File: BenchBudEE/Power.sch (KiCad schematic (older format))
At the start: 0 parts

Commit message: swapping Power and PowerAdjustmentMonitor schematics
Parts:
- added C?: 5566-20A, ~, symbol 5566-20A
- added F? (x6): FUSE, ~, symbol FUSE
- added SW?: SWITCH_INV, ~, symbol SWITCH_INV
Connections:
- new net: C?.1 (+3.3V), C?.11 (+3.3V_SENSE), C?.2 (+3.3V), F?.1
- new net: C?.10 (+12V), F?.2
- new net: C?.12 (-12V), F?.1
- new net: C?.18 (-5V_OPT), F?.1
- new net: C?.19 (+5V), C?.20 (+5V), C?.4 (+5V), C?.6 (+5V), F?.2
- new net +12V: F?.1
- new net +3.3V: F?.2
- new net +5V: F?.1
- new net -12V: F?.2
- new net -5V: F?.2
- new net GND: C?.13 (GND), C?.15 (GND), C?.16 (GND), C?.17 (GND), C?.3 (GND), C?.5 (GND), C?.7 (GND)

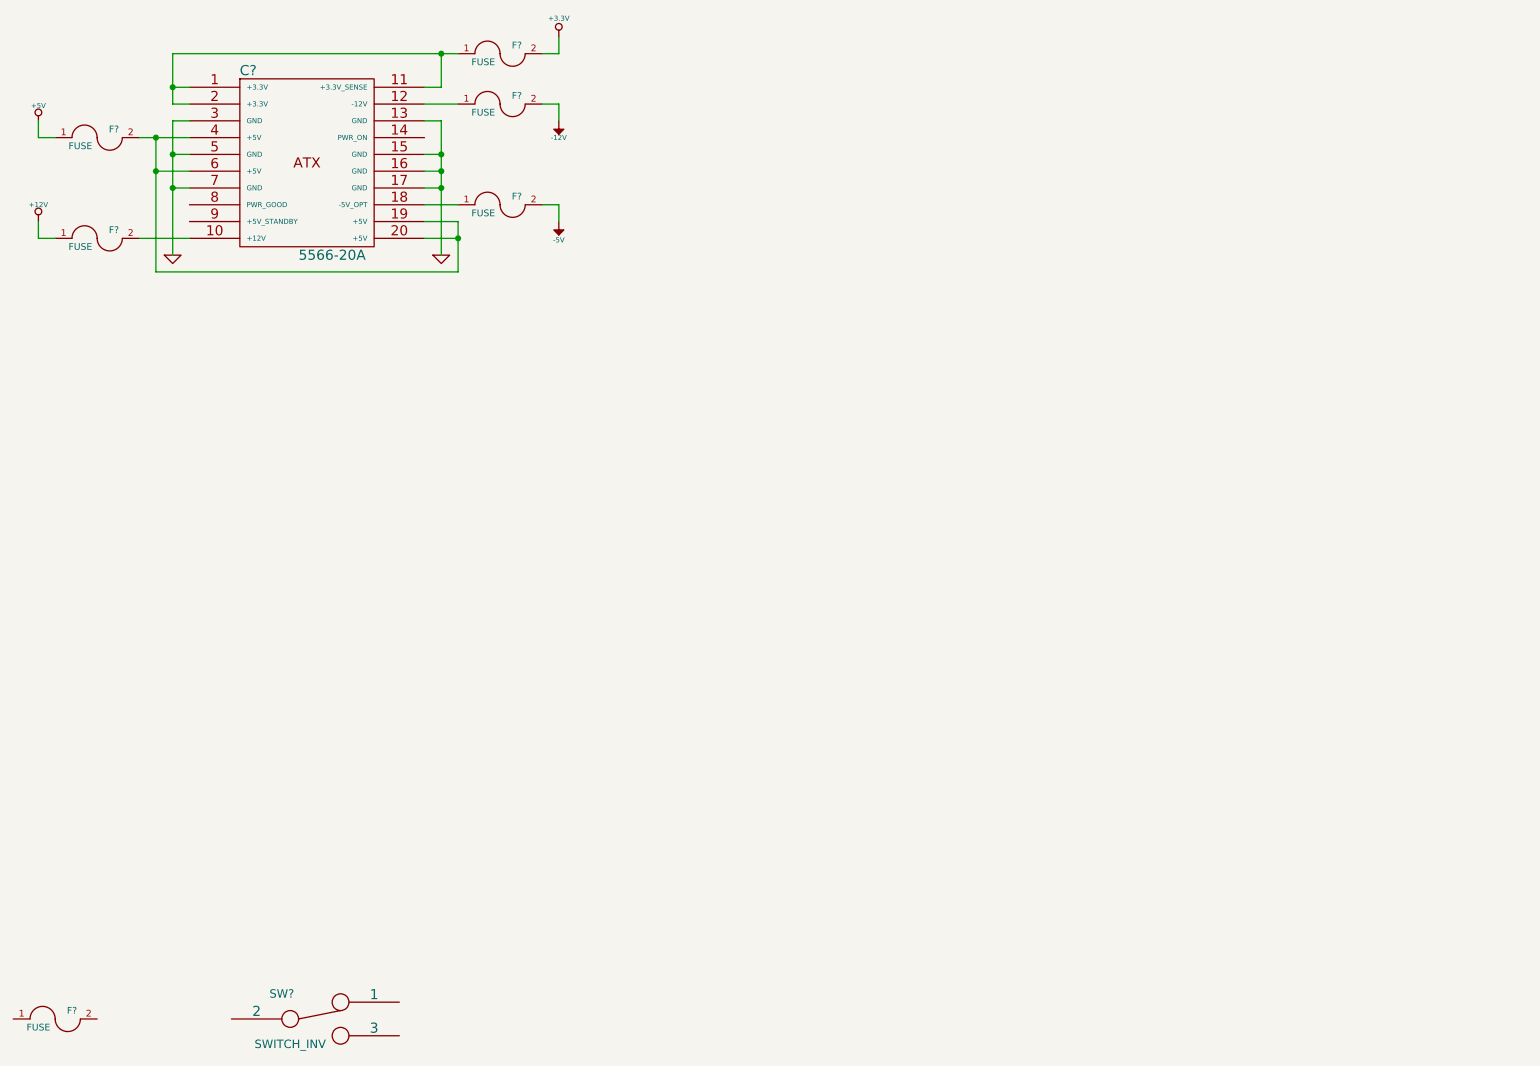
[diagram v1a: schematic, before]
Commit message: Implementing the Power schematic.
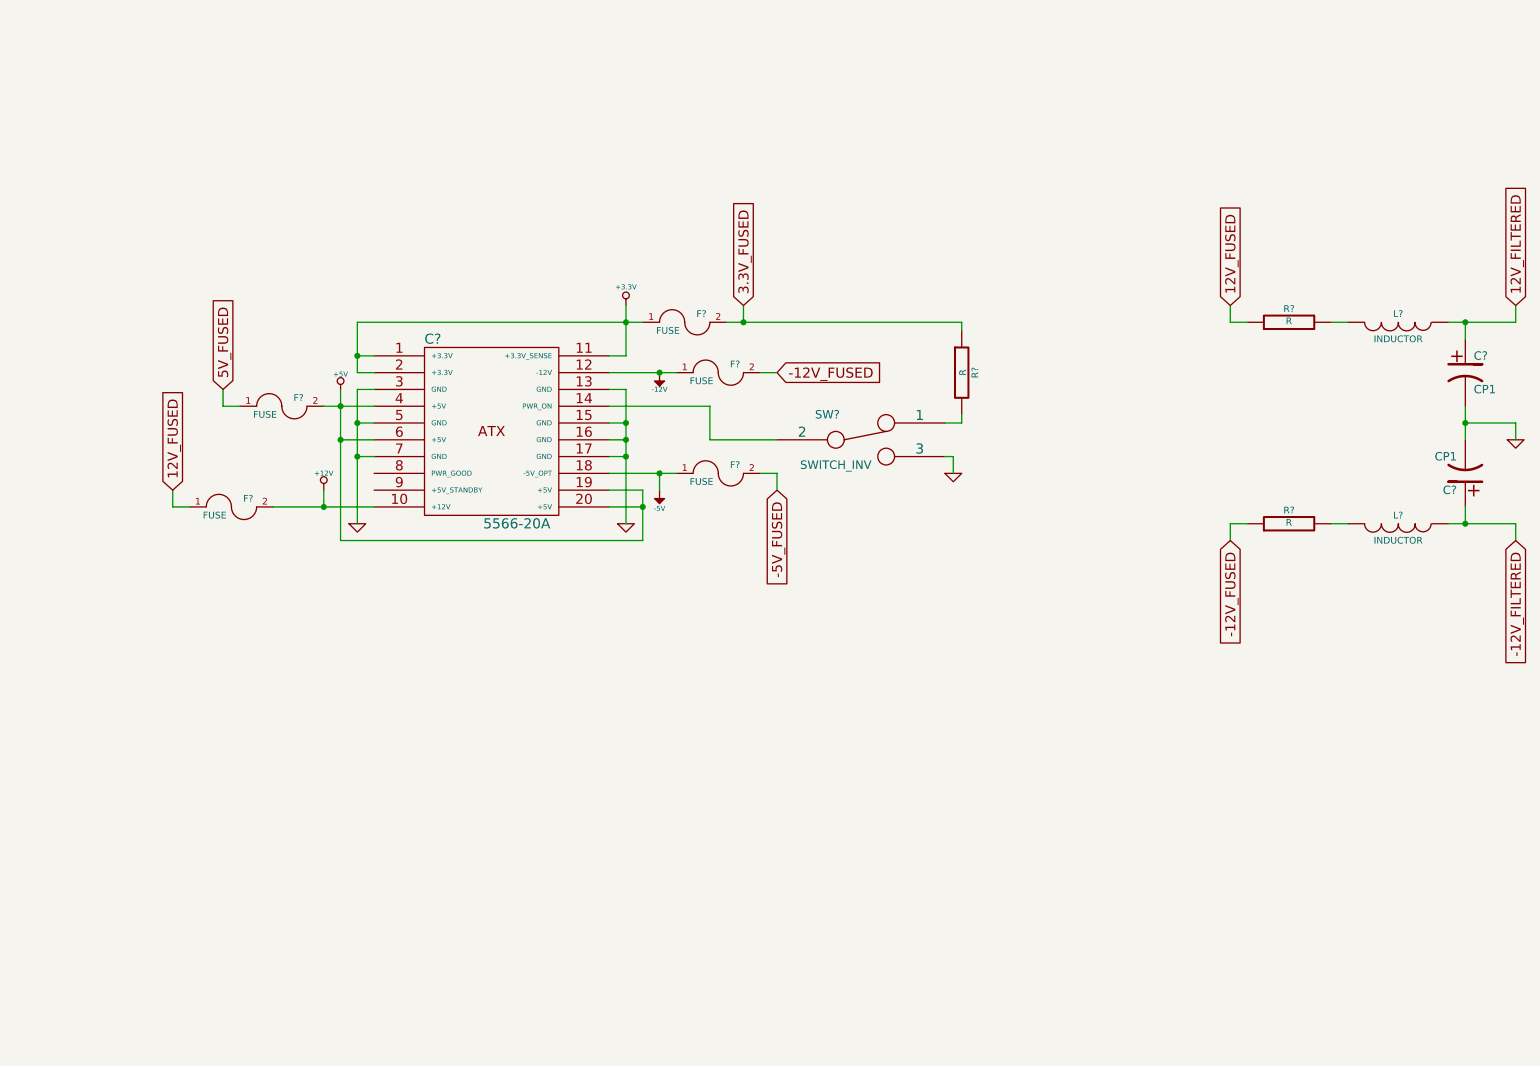
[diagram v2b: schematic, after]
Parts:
- removed F?: FUSE, ~, symbol FUSE
- added C? (x2): CP1, ~, symbol CP1
- added L? (x2): INDUCTOR, ~, symbol INDUCTOR
- added R? (x3): R, ~, symbol R
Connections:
- net +12V: now also C?.10 (+12V), F?.2; no longer F?.1
- net +3.3V: now also C?.1 (+3.3V), C?.11 (+3.3V_SENSE), C?.2 (+3.3V), F?.1; no longer F?.2
- net +5V: now also C?.19 (+5V), C?.20 (+5V), C?.4 (+5V), C?.6 (+5V), F?.2; no longer F?.1
- net -12V: now also C?.12 (-12V), F?.1; no longer F?.2
- net -5V: now also C?.18 (-5V_OPT), F?.1; no longer F?.2
- net GND: now also SW?.3, C?.2, C?.2
- net at C?.14 (PWR_ON): now also SW?.2
- net at SW?.1: now also R?.2
- new net: L?.2, R?.2 (x2)
- new net -12V_FILTERED: C?.1, L?.1
- new net -12V_FUSED: F?.2, R?.1
- new net -5V_FUSED: F?.2
- new net 12V_FILTERED: C?.1, L?.1
- new net 12V_FUSED: F?.1, R?.1
- new net 3.3V_FUSED: F?.2, R?.1
- new net 5V_FUSED: F?.1
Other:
- moved on the sheet: C?, F?, SW?

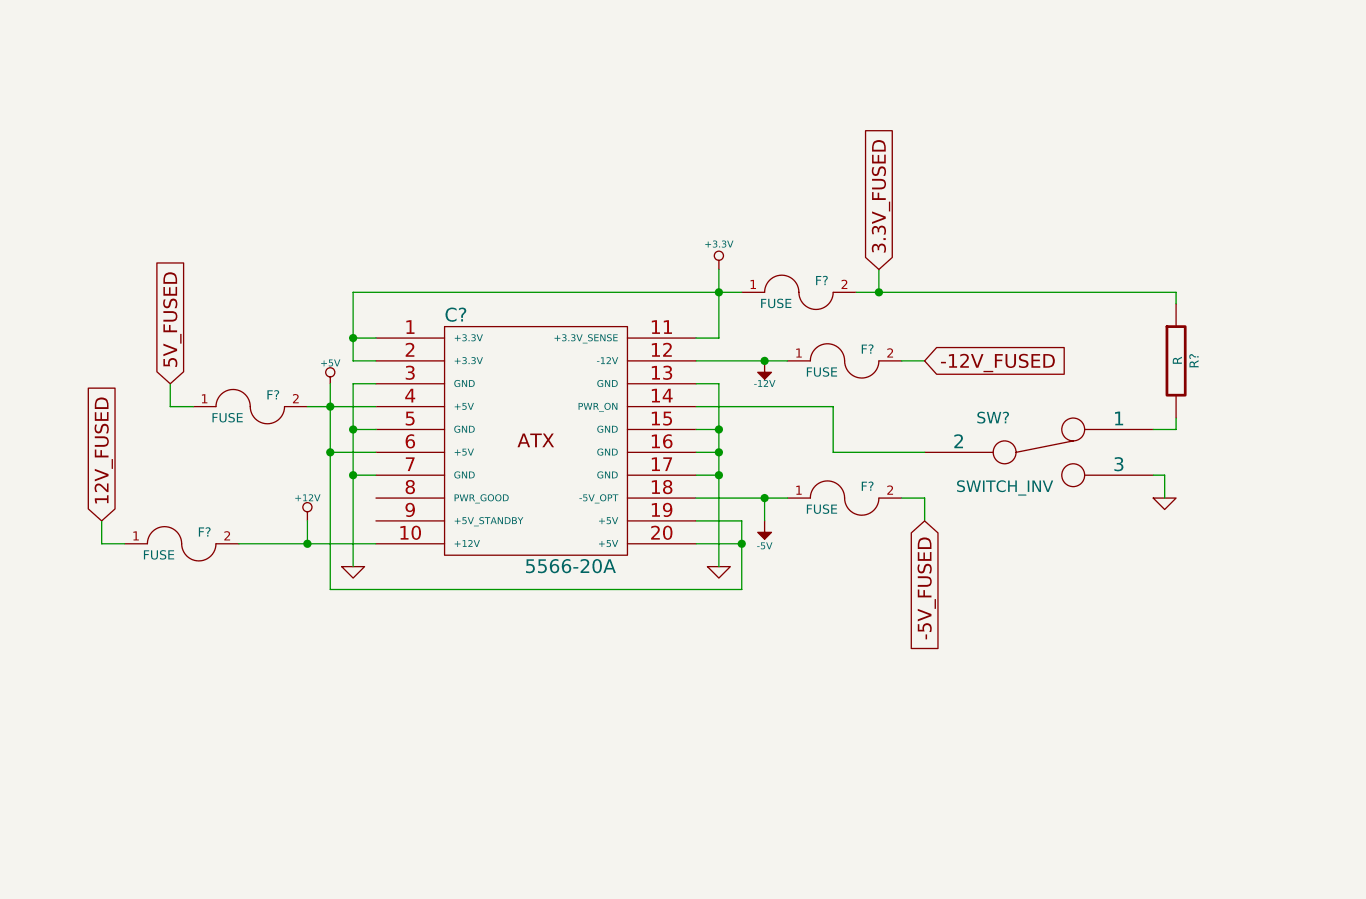
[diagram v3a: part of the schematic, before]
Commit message: Completing schematics from week 3 videos.
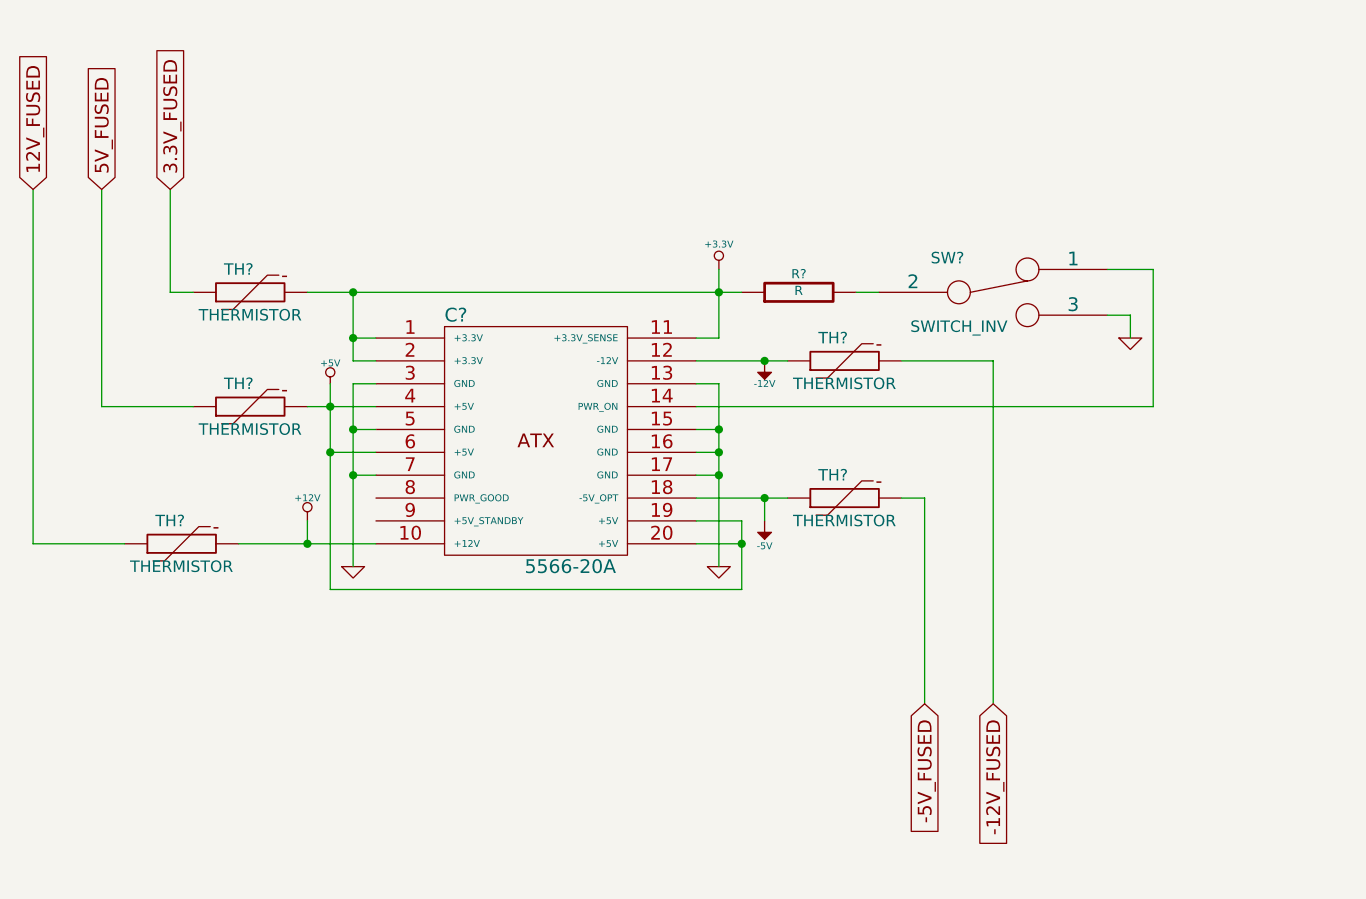
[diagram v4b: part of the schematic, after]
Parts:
- removed F? (x5): FUSE, ~, symbol FUSE
- added TH? (x5): THERMISTOR, ~, symbol THERMISTOR
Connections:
- net +12V: now also TH?.2
- net +3.3V: now also R?.1, TH?.2
- net +5V: now also TH?.2
- net -12V: now also TH?.1
- net -12V_FUSED: now also TH?.2
- net -5V: now also TH?.1
- net -5V_FUSED: now also TH?.2
- net 12V_FUSED: now also TH?.1
- net 3.3V_FUSED: now also TH?.1; no longer R?.1
- net 5V_FUSED: now also TH?.1
- net at C?.14 (PWR_ON): now also SW?.1; no longer SW?.2
- net at R?.2: now also SW?.2; no longer SW?.1
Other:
- moved on the sheet: R?, SW?
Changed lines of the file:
@@
 LIBS:relay_spdt
 LIBS:5566-20A
+LIBS:AP5726
+LIBS:arduino
 LIBS:BenchBudEE-cache
 EELAYER 27 0
@@
 $Descr A4 11693 8268
 encoding utf-8
-Sheet 5 9
+Sheet 4 9
 Title ""
-Date "13 feb 2014"
+Date "24 feb 2014"
 Rev ""
 Comp ""
@@
 L SWITCH_INV SW?
 U 1 1 52FAF3C7
-P 6050 3800
-F 0 "SW?" H 5850 3950 50  0000 C CNN
-F 1 "SWITCH_INV" H 5900 3650 50  0000 C CNN
-F 2 "~" H 6050 3800 60  0000 C CNN
-F 3 "~" H 6050 3800 60  0000 C CNN
-	1    6050 3800
-	1    0    0    -1
-$EndComp
-$Comp
-L FUSE F?
-U 1 1 52FAF3D4
-P 5000 3100
-F 0 "F?" H 5100 3150 40  0000 C CNN
-F 1 "FUSE" H 4900 3050 40  0000 C CNN
-F 2 "~" H 5000 3100 60  0000 C CNN
-F 3 "~" H 5000 3100 60  0000 C CNN
-	1    5000 3100
-	1    0    0    -1
-$EndComp
-$Comp
-L FUSE F?
-U 1 1 52FAF44C
-P 2600 3600
-F 0 "F?" H 2700 3650 40  0000 C CNN
-F 1 "FUSE" H 2500 3550 40  0000 C CNN
-F 2 "~" H 2600 3600 60  0000 C CNN
-F 3 "~" H 2600 3600 60  0000 C CNN
-	1    2600 3600
-	1    0    0    -1
-$EndComp
-$Comp
-L FUSE F?
-U 1 1 52FAF521
-P 2300 4200
-F 0 "F?" H 2400 4250 40  0000 C CNN
-F 1 "FUSE" H 2200 4150 40  0000 C CNN
-F 2 "~" H 2300 4200 60  0000 C CNN
-F 3 "~" H 2300 4200 60  0000 C CNN
-	1    2300 4200
-	1    0    0    -1
-$EndComp
-$Comp
-L FUSE F?
-U 1 1 52FAF58B
-P 5200 3400
-F 0 "F?" H 5300 3450 40  0000 C CNN
-F 1 "FUSE" H 5100 3350 40  0000 C CNN
-F 2 "~" H 5200 3400 60  0000 C CNN
-F 3 "~" H 5200 3400 60  0000 C CNN
-	1    5200 3400
-	1    0    0    -1
-$EndComp
-$Comp
-L FUSE F?
-U 1 1 52FAF5CF
-P 5200 4000
-F 0 "F?" H 5300 4050 40  0000 C CNN
-F 1 "FUSE" H 5100 3950 40  0000 C CNN
-F 2 "~" H 5200 4000 60  0000 C CNN
-F 3 "~" H 5200 4000 60  0000 C CNN
-	1    5200 4000
+P 5850 3100
+F 0 "SW?" H 5650 3250 50  0000 C CNN
+F 1 "SWITCH_INV" H 5700 2950 50  0000 C CNN
+F 2 "~" H 5850 3100 60  0000 C CNN
+F 3 "~" H 5850 3100 60  0000 C CNN
+	1    5850 3100
 	1    0    0    -1
 $EndComp
@@
 L GND #PWR?
 U 1 1 52FAED7C
-P 6600 4000
-F 0 "#PWR?" H 6600 4000 30  0001 C CNN
-F 1 "GND" H 6600 3930 30  0001 C CNN
-F 2 "" H 6600 4000 60  0000 C CNN
-F 3 "" H 6600 4000 60  0000 C CNN
-	1    6600 4000
+P 6450 3300
+F 0 "#PWR?" H 6450 3300 30  0001 C CNN
+F 1 "GND" H 6450 3230 30  0001 C CNN
+F 2 "" H 6450 3300 60  0000 C CNN
+F 3 "" H 6450 3300 60  0000 C CNN
+	1    6450 3300
 	1    0    0    -1
 $EndComp
@@
 L R R?
 U 1 1 52FAEDB5
-P 6650 3400
-F 0 "R?" V 6730 3400 40  0000 C CNN
-F 1 "R" V 6657 3401 40  0000 C CNN
-F 2 "~" V 6580 3400 30  0000 C CNN
-F 3 "~" H 6650 3400 30  0000 C CNN
-	1    6650 3400
-	1    0    0    -1
+P 5000 3100
+F 0 "R?" V 5080 3100 40  0000 C CNN
+F 1 "R" V 5007 3101 40  0000 C CNN
+F 2 "~" V 4930 3100 30  0000 C CNN
+F 3 "~" H 5000 3100 30  0000 C CNN
+	1    5000 3100
+	0    -1   -1   0
 $EndComp
 $Comp
@@
 	3050 3400 3050 3100
 Wire Wire Line
-	3050 3100 4750 3100
+	2850 3100 4750 3100
 Wire Wire Line
 	3150 3300 3050 3300
@@
 	4650 3000 4650 3300
 Wire Wire Line
-	5250 3100 6650 3100
-Wire Wire Line
 	2950 3500 2950 4400
 Wire Wire Line
@@
 	4550 4000 4950 4000
 Wire Wire Line
-	5150 3600 5150 3800
-Wire Wire Line
-	5150 3600 4550 3600
+	4550 3600 6550 3600
 Wire Wire Line
 	9650 4200 9650 4300
@@
 	8950 4300 8850 4300
 Wire Wire Line
-	2350 3600 2250 3600
-Wire Wire Line
-	2250 3600 2250 3500
-Text GLabel 2250 3500 1    60   Input ~ 0
+	1950 3600 2350 3600
+Text GLabel 1950 2650 1    60   Input ~ 0
 5V_FUSED
 Wire Wire Line
@@
 	2850 4200 2850 4100
 Connection ~ 2850 4200
-Text GLabel 1950 4100 1    60   Input ~ 0
+Text GLabel 1650 2650 1    60   Input ~ 0
 12V_FUSED
 Wire Wire Line
-	2050 4200 1950 4200
-Wire Wire Line
-	1950 4200 1950 4100
-Wire Wire Line
-	5350 3100 5350 3000
-Connection ~ 5350 3100
-Text GLabel 5350 3000 1    60   Input ~ 0
+	1650 4200 2050 4200
+Text GLabel 2250 2650 1    60   Input ~ 0
 3.3V_FUSED
 Connection ~ 4850 3400
 Wire Wire Line
-	5450 3400 5550 3400
-Text GLabel 5550 3400 2    60   Input ~ 0
+	5450 3400 5850 3400
+Text GLabel 5850 4900 3    60   Input ~ 0
 -12V_FUSED
-Wire Wire Line
-	5150 3800 5550 3800
-Wire Wire Line
-	6550 3900 6600 3900
-Wire Wire Line
-	6600 3900 6600 4000
-Wire Wire Line
-	6650 3700 6550 3700
-Wire Wire Line
-	6650 3100 6650 3150
-Wire Wire Line
-	6650 3650 6650 3700
 Wire Wire Line
 	4850 4000 4850 4100
@@
 	5450 4000 5550 4000
 Wire Wire Line
-	5550 4000 5550 4100
-Text GLabel 5550 4100 3    60   Input ~ 0
+	5550 4000 5550 4900
+Text GLabel 5550 4900 3    60   Input ~ 0
 -5V_FUSED
 Wire Wire Line
@@
 Text GLabel 9950 4400 3    60   Input ~ 0
 -12V_FILTERED
+$Comp
+L THERMISTOR TH?
+U 1 1 53094891
+P 2600 3600
+F 0 "TH?" V 2700 3650 50  0000 C CNN
+F 1 "THERMISTOR" V 2500 3600 50  0000 C CNN
+F 2 "~" H 2600 3600 60  0000 C CNN
+F 3 "~" H 2600 3600 60  0000 C CNN
+	1    2600 3600
+	0    -1   -1   0
+$EndComp
+$Comp
+L THERMISTOR TH?
+U 1 1 530948AA
+P 2300 4200
+F 0 "TH?" V 2400 4250 50  0000 C CNN
+F 1 "THERMISTOR" V 2200 4200 50  0000 C CNN
+F 2 "~" H 2300 4200 60  0000 C CNN
+F 3 "~" H 2300 4200 60  0000 C CNN
+	1    2300 4200
+	0    -1   -1   0
+$EndComp
+$Comp
+L THERMISTOR TH?
+U 1 1 530949A6
+P 2600 3100
+F 0 "TH?" V 2700 3150 50  0000 C CNN
+F 1 "THERMISTOR" V 2500 3100 50  0000 C CNN
+F 2 "~" H 2600 3100 60  0000 C CNN
+F 3 "~" H 2600 3100 60  0000 C CNN
+	1    2600 3100
+	0    -1   -1   0
+$EndComp
+$Comp
+L THERMISTOR TH?
+U 1 1 530949B5
+P 5200 3400
+F 0 "TH?" V 5300 3450 50  0000 C CNN
+F 1 "THERMISTOR" V 5100 3400 50  0000 C CNN
+F 2 "~" H 5200 3400 60  0000 C CNN
+F 3 "~" H 5200 3400 60  0000 C CNN
+	1    5200 3400
+	0    -1   -1   0
+$EndComp
+$Comp
+L THERMISTOR TH?
+U 1 1 530949C4
+P 5200 4000
+F 0 "TH?" V 5300 4050 50  0000 C CNN
+F 1 "THERMISTOR" V 5100 4000 50  0000 C CNN
+F 2 "~" H 5200 4000 60  0000 C CNN
+F 3 "~" H 5200 4000 60  0000 C CNN
+	1    5200 4000
+	0    -1   -1   0
+$EndComp
+Wire Wire Line
+	5850 3400 5850 4900
+Connection ~ 3050 3100
+Wire Wire Line
+	2250 2650 2250 3100
+Wire Wire Line
+	2250 3100 2350 3100
+Wire Wire Line
+	1950 3600 1950 2650
+Wire Wire Line
+	1650 4200 1650 2650
+Wire Wire Line
+	5250 3100 5350 3100
+Wire Wire Line
+	6350 3200 6450 3200
+Wire Wire Line
+	6450 3200 6450 3300
+Wire Wire Line
+	6350 3000 6550 3000
+Wire Wire Line
+	6550 3000 6550 3600
 $EndSCHEMATC
